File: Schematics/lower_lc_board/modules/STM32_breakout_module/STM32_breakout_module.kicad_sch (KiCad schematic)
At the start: 56 parts, among them J2 SWD_CONN, J3 USB_C_CONN, Q4 2N7002, SW1 SW_STM_RESET, SW2 SW_STM_BOOT_MODE, U5 STM32F103CBT6, U6 W25Q128JVS, U7 ISO1044BDR, U8 CP2102N-Axx-xQFN20, Y1 X322516MMB4SI

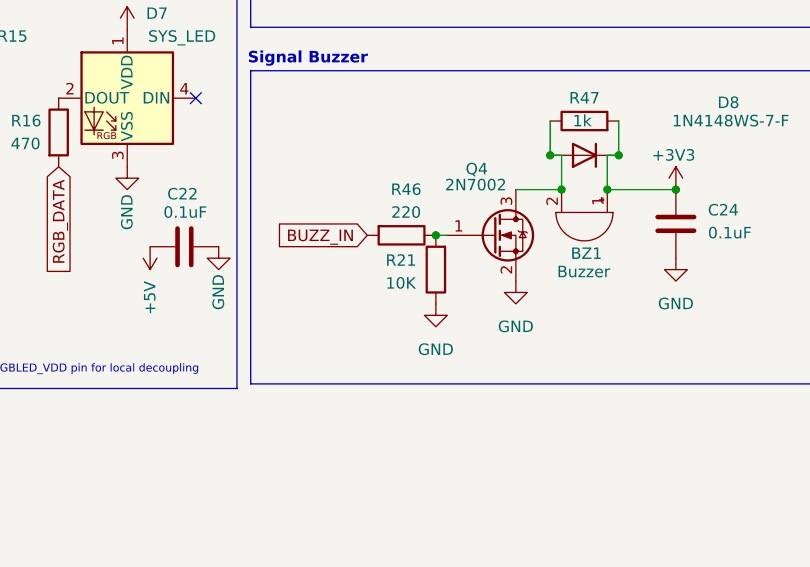
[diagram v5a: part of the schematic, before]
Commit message: increase width on power rails from USB and SWD, start tuning diff pairs
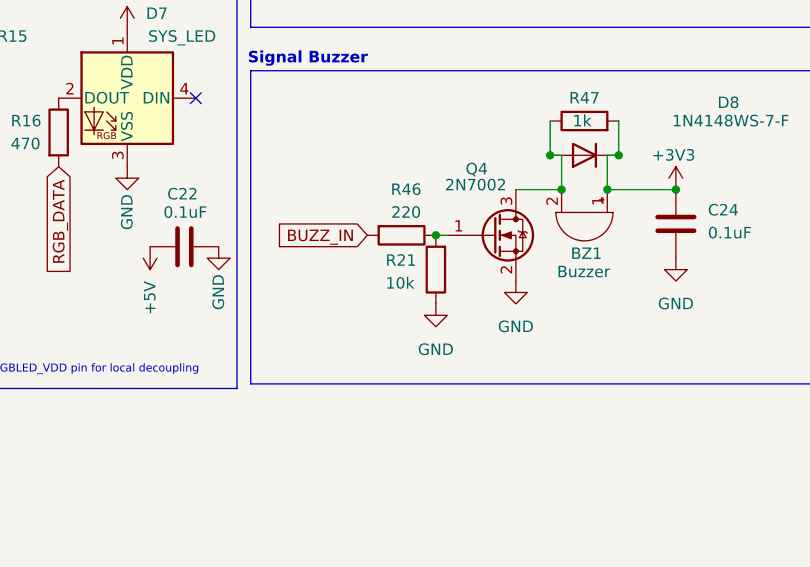
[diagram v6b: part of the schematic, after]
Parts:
- C13, C14: footprint Capacitor_SMD:C_0603_1608Metric -> Capacitor_SMD:C_0402_1005Metric; JLCPCB C14663 -> C1525
- C20: footprint Capacitor_SMD:C_0603_1608Metric -> Capacitor_SMD:C_0402_1005Metric; JLCPCB C15849 -> C52923
- D5, D6: JLCPCB (none) -> C2290
- R11: footprint Resistor_SMD:R_0603_1608Metric -> Resistor_SMD:R_0402_1005Metric; JLCPCB C31850 -> C25768
- R12: footprint Resistor_SMD:R_0603_1608Metric -> Resistor_SMD:R_0402_1005Metric; JLCPCB C25819 -> C25792
- R13: JLCPCB C21190 -> C4410
- R15: JLCPCB C22808 -> C22962
- R21: value 10K -> 10k
- R45: footprint Resistor_SMD:R_0603_1608Metric -> Capacitor_SMD:C_0402_1005Metric; JLCPCB C22843 -> C25867
- R47: JLCPCB (none) -> C21190
- U7: Digikey (none) -> 296-ISO1044BD-ND
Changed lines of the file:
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@@
 			)
 		)
-		(property "Value" "10K"
+		(property "Value" "10k"
 			(at 224.282 145.034 0)
 			(effects
@@
 			)
 		)
-		(property "JLCPCB" "C22808"
+		(property "JLCPCB" "C22962"
 			(at 179.07 118.11 0)
 			(effects
@@
 			)
 		)
-		(property "Footprint" "Capacitor_SMD:C_0603_1608Metric"
+		(property "Footprint" "Capacitor_SMD:C_0402_1005Metric"
 			(at 45.4152 158.75 0)
 			(effects
@@
 			)
 		)
-		(property "JLCPCB" "C14663"
+		(property "JLCPCB" "C1525"
 			(at 44.45 154.94 0)
 			(effects
@@
 			)
 		)
+		(property "Digikey" "296-ISO1044BD-ND"
+			(at 177.8 87.63 0)
+			(effects
+				(font
+					(size 1.27 1.27)
+				)
+				(hide yes)
+			)
+		)
 		(pin "2"
 		)
@@
 			)
 		)
+		(property "JLCPCB" "C21190"
+			(at 246.38 127 0)
+			(effects
+				(font
+					(size 1.27 1.27)
+				)
+				(hide yes)
+			)
+		)
 		(pin "1"
 		)
@@
 			)
 		)
-		(property "Footprint" "Capacitor_SMD:C_0603_1608Metric"
+		(property "Footprint" "Capacitor_SMD:C_0402_1005Metric"
 			(at 35.2552 158.75 0)
 			(effects
@@
 			)
 		)
-		(property "JLCPCB" "C14663"
+		(property "JLCPCB" "  C1525"
 			(at 34.29 154.94 0)
 			(effects
@@
 			)
 		)
+		(property "JLCPCB" "C2290"
+			(at 179.07 125.73 0)
+			(effects
+				(font
+					(size 1.27 1.27)
+				)
+				(hide yes)
+			)
+		)
 		(pin "2"
 		)
@@
 			)
 		)
-		(property "Footprint" "Capacitor_SMD:C_0603_1608Metric"
+		(property "Footprint" "Capacitor_SMD:C_0402_1005Metric"
 			(at 225.0948 59.69 0)
 			(effects
@@
 			)
 		)
-		(property "JLCPCB" "C15849"
+		(property "JLCPCB" "C52923"
 			(at 226.06 63.5 0)
 			(effects
@@
 			)
 		)
-		(property "Footprint" "Resistor_SMD:R_0603_1608Metric"
+		(property "Footprint" "Resistor_SMD:R_0402_1005Metric"
 			(at 217.678 63.5 90)
 			(effects
@@
 			)
 		)
-		(property "JLCPCB" "C25819 "
+		(property "JLCPCB" "C25792"
 			(at 215.9 63.5 0)
 			(effects
@@
 			)
 		)
-		(property "Footprint" "Resistor_SMD:R_0603_1608Metric"
+		(property "Footprint" "Resistor_SMD:R_0402_1005Metric"
 			(at 217.678 55.88 90)
 			(effects
@@
 			)
 		)
-		(property "JLCPCB" "C31850"
+		(property "JLCPCB" "C25768 "
 			(at 215.9 55.88 0)
 			(effects
@@
 			)
 		)
-		(property "JLCPCB" "C21190"
+		(property "JLCPCB" "C4410"
 			(at 231.14 46.99 0)
 			(effects
@@
 			)
 		)
+		(property "JLCPCB" "C2290"
+			(at 160.02 125.73 0)
+			(effects
+				(font
+					(size 1.27 1.27)
+				)
+				(hide yes)
+			)
+		)
 		(pin "2"
 		)
@@
 			)
 		)
-		(property "Footprint" "Resistor_SMD:R_0603_1608Metric"
+		(property "Footprint" "Capacitor_SMD:C_0402_1005Metric"
 			(at 135.382 140.97 90)
 			(effects
@@
 			)
 		)
-		(property "JLCPCB" "C22843"
+		(property "JLCPCB" "C25867"
 			(at 137.16 140.97 0)
 			(effects

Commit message: start lower refactor
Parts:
- removed C12: 10uF, Capacitor_SMD:CP_Elec_4x5.4, symbol Device:C_Polarized
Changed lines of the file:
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@@
 	)
 	(junction
-		(at 34.29 151.13)
-		(diameter 0)
-		(color 0 0 0 0)
-	)
-	(junction
-		(at 26.67 158.75)
-		(diameter 0)
-		(color 0 0 0 0)
-	)
-	(junction
 		(at 134.62 74.93)
 		(diameter 0)
@@
 	(wire
 		(pts
-			(xy 26.67 158.75) (xy 34.29 158.75)
-		)
-		(stroke
-			(width 0)
-			(type default)
-		)
-	)
-	(wire
-		(pts
 			(xy 248.92 134.62) (xy 256.54 134.62)
 		)
@@
 	(wire
 		(pts
-			(xy 26.67 158.75) (xy 26.67 161.29)
+			(xy 34.29 158.75) (xy 34.29 161.29)
 		)
 		(stroke
@@
 	(wire
 		(pts
-			(xy 26.67 151.13) (xy 34.29 151.13)
-		)
-		(stroke
-			(width 0)
-			(type default)
-		)
-	)
-	(wire
-		(pts
 			(xy 133.35 135.89) (xy 134.62 135.89)
 		)
@@
 	)
 	(symbol
-		(lib_id "Device:C_Polarized")
-		(at 26.67 154.94 0)
-		(unit 1)
-		(exclude_from_sim no)
-		(in_bom yes)
-		(on_board yes)
-		(dnp no)
-		(property "Reference" "C12"
-			(at 20.32 153.035 0)
-			(effects
-				(font
-					(size 1.27 1.27)
-				)
-				(justify left)
-			)
-		)
-		(property "Value" "10uF"
-			(at 18.415 155.4592 0)
-			(effects
-				(font
-					(size 1.27 1.27)
-				)
-				(justify left)
-			)
-		)
-		(property "Footprint" "Capacitor_SMD:CP_Elec_4x5.4"
-			(at 27.6352 158.75 0)
-			(effects
-				(font
-					(size 1.27 1.27)
-				)
-				(hide yes)
-			)
-		)
-		(property "Datasheet" "https://www.we-online.com/components/products/datasheet/865080340001.pdf"
-			(at 26.67 154.94 0)
-			(effects
-				(font
-					(size 1.27 1.27)
-				)
-				(hide yes)
-			)
-		)
-		(property "Description" ""
-			(at 26.67 154.94 0)
-			(effects
-				(font
-					(size 1.27 1.27)
-				)
-				(hide yes)
-			)
-		)
-		(property "Digikey" "732-8411-1-ND"
-			(at 26.67 154.94 0)
-			(effects
-				(font
-					(size 1.27 1.27)
-				)
-				(hide yes)
-			)
-		)
-		(pin "1"
-		)
-		(pin "2"
-		)
-		(instances
-			(project "lower_lc_board"
-				(path "/d63798c4-e363-437e-9012-e4aff32e6642/925ef91a-c900-4b94-a159-606c279d7192"
-					(reference "C12")
-					(unit 1)
-				)
-			)
-		)
-	)
-	(symbol
 		(lib_id "power:+3V3")
 		(at 165.1 85.09 90)
@@
 	(symbol
 		(lib_id "power:GND")
-		(at 26.67 161.29 0)
+		(at 34.29 161.29 0)
 		(unit 1)
 		(exclude_from_sim no)
@@
 		(fields_autoplaced yes)
 		(property "Reference" "#PWR028"
-			(at 26.67 167.64 0)
+			(at 34.29 167.64 0)
 			(effects
 				(font
@@
 		)
 		(property "Value" "GND"
-			(at 26.67 165.735 0)
+			(at 34.29 165.735 0)
 			(effects
 				(font
@@
 		)
 		(property "Footprint" ""
-			(at 26.67 161.29 0)
+			(at 34.29 161.29 0)
 			(effects
 				(font
@@
 		)
 		(property "Datasheet" ""
-			(at 26.67 161.29 0)
+			(at 34.29 161.29 0)
 			(effects
 				(font
@@
 		)
 		(property "Description" ""
-			(at 26.67 161.29 0)
+			(at 34.29 161.29 0)
 			(effects
 				(font
